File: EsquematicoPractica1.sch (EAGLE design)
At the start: 47 parts, among them IC1 GSOT05C-GS08, Q1 IRF7416PBF, Q2 IRF7416PBF, U1 MKL27Z64VLH4, U2 SFH6156-4TSMD-4_VO-L, U3 MC34063ADR, U4 SFH6156-4TSMD-4_VO-L, U5 SFH6156-4TSMD-4_VO-L, U6 SFH6156-4TSMD-4_VO-L, U7 5002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

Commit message: [Code] JTAG interface without pin connections
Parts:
- added J1: M50-3500542, M50-3500542:M50-3500542
- added R16: 10K, rcl:R-US_M1206
- renumbered U7 to TP5
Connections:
- new net N$32: R15.2
- new net N$33: R14.1
- new net N$34: J1.2, R16.1
- new net N$36: J1.4
- new net N$37: J1.6
- new net N$38: J1.8
- new net N$39: J1.10
- new net N$40: J1.1
- net GND: now also J1.3, J1.5
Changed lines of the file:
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@@
 <part name="GND12" library="supply1" library_urn="urn:adsk.eagle:library:371" deviceset="GND" device=""/>
 <part name="IC1" library="GSOT05C-GS08" deviceset="GSOT05C-GS08" device=""/>
-<part name="U7" library="5002" deviceset="5002" device=""/>
+<part name="TP5" library="5002" deviceset="5002" device=""/>
+<part name="R16" library="rcl" library_urn="urn:adsk.eagle:library:334" deviceset="R-US_" device="M1206" package3d_urn="urn:adsk.eagle:package:23566/1" value="10K"/>
+<part name="GND13" library="supply1" library_urn="urn:adsk.eagle:library:371" deviceset="GND" device=""/>
+<part name="J1" library="M50-3500542" deviceset="M50-3500542" device=""/>
 </parts>
 <sheets>
@@
 <sheet>
 <plain>
-<wire x1="129.54" y1="568.96" x2="1201.42" y2="568.96" width="0.1524" layer="97"/>
-<wire x1="129.54" y1="568.96" x2="129.54" y2="-160.02" width="0.1524" layer="97"/>
-<wire x1="129.54" y1="-160.02" x2="1201.42" y2="-160.02" width="0.1524" layer="97"/>
-<wire x1="1201.42" y1="568.96" x2="1201.42" y2="-160.02" width="0.1524" layer="97"/>
+<wire x1="129.54" y1="568.96" x2="264.16" y2="568.96" width="0.1524" layer="97"/>
+<wire x1="129.54" y1="568.96" x2="129.54" y2="439.42" width="0.1524" layer="97"/>
+<wire x1="129.54" y1="439.42" x2="264.16" y2="439.42" width="0.1524" layer="97"/>
+<wire x1="264.16" y1="568.96" x2="264.16" y2="439.42" width="0.1524" layer="97"/>
+<wire x1="266.7" y1="568.96" x2="401.32" y2="568.96" width="0.1524" layer="97"/>
+<wire x1="266.7" y1="568.96" x2="266.7" y2="439.42" width="0.1524" layer="97"/>
+<wire x1="266.7" y1="439.42" x2="401.32" y2="439.42" width="0.1524" layer="97"/>
+<wire x1="401.32" y1="568.96" x2="401.32" y2="439.42" width="0.1524" layer="97"/>
 </plain>
 <instances>
@@
 <instance part="GND12" gate="1" x="210.82" y="553.72" rot="R180"/>
 <instance part="IC1" gate="G$1" x="210.82" y="510.54" rot="R90"/>
-<instance part="U7" gate="G$1" x="213.36" y="482.6" rot="R270"/>
+<instance part="TP5" gate="G$1" x="213.36" y="482.6" rot="R270"/>
+<instance part="R16" gate="G$1" x="365.76" y="508" rot="R90"/>
+<instance part="GND13" gate="1" x="320.04" y="485.14"/>
+<instance part="J1" gate="G$1" x="325.12" y="500.38"/>
 </instances>
 <busses>
@@
 <junction x="210.82" y="551.18"/>
 </segment>
+<segment>
+<pinref part="J1" gate="G$1" pin="3"/>
+<wire x1="325.12" y1="497.84" x2="320.04" y2="497.84" width="0.1524" layer="91"/>
+<wire x1="320.04" y1="497.84" x2="320.04" y2="495.3" width="0.1524" layer="91"/>
+<pinref part="J1" gate="G$1" pin="5"/>
+<wire x1="320.04" y1="495.3" x2="320.04" y2="487.68" width="0.1524" layer="91"/>
+<wire x1="325.12" y1="495.3" x2="320.04" y2="495.3" width="0.1524" layer="91"/>
+<junction x="320.04" y="495.3"/>
+<pinref part="GND13" gate="1" pin="GND"/>
+</segment>
 </net>
 <net name="N$26" class="0">
 <segment>
 <pinref part="L3" gate="G$1" pin="2"/>
-<pinref part="U7" gate="G$1" pin="1"/>
+<pinref part="TP5" gate="G$1" pin="1"/>
 <wire x1="205.74" y1="482.6" x2="213.36" y2="482.6" width="0.1524" layer="91"/>
-<wire x1="213.36" y1="482.6" x2="236.22" y2="482.6" width="0.1524" layer="91"/>
+<wire x1="213.36" y1="482.6" x2="248.92" y2="482.6" width="0.1524" layer="91"/>
 <junction x="213.36" y="482.6"/>
 </segment>
 </net>
+<net name="N$32" class="0">
+<segment>
+<pinref part="R15" gate="G$1" pin="2"/>
+<wire x1="228.6" y1="497.84" x2="248.92" y2="497.84" width="0.1524" layer="91"/>
+</segment>
+</net>
+<net name="N$33" class="0">
+<segment>
+<pinref part="R14" gate="G$1" pin="1"/>
+<wire x1="236.22" y1="492.76" x2="248.92" y2="492.76" width="0.1524" layer="91"/>
+</segment>
+</net>
+<net name="N$34" class="0">
+<segment>
+<pinref part="J1" gate="G$1" pin="2"/>
+<pinref part="R16" gate="G$1" pin="1"/>
+<wire x1="347.98" y1="500.38" x2="365.76" y2="500.38" width="0.1524" layer="91"/>
+<wire x1="365.76" y1="500.38" x2="365.76" y2="502.92" width="0.1524" layer="91"/>
+<wire x1="365.76" y1="500.38" x2="381" y2="500.38" width="0.1524" layer="91"/>
+<junction x="365.76" y="500.38"/>
+</segment>
+</net>
+<net name="N$36" class="0">
+<segment>
+<pinref part="J1" gate="G$1" pin="4"/>
+<wire x1="347.98" y1="497.84" x2="381" y2="497.84" width="0.1524" layer="91"/>
+</segment>
+</net>
+<net name="N$37" class="0">
+<segment>
+<pinref part="J1" gate="G$1" pin="6"/>
+<wire x1="347.98" y1="495.3" x2="381" y2="495.3" width="0.1524" layer="91"/>
+</segment>
+</net>
+<net name="N$38" class="0">
+<segment>
+<pinref part="J1" gate="G$1" pin="8"/>
+<wire x1="347.98" y1="492.76" x2="381" y2="492.76" width="0.1524" layer="91"/>
+</segment>
+</net>
+<net name="N$39" class="0">
+<segment>
+<pinref part="J1" gate="G$1" pin="10"/>
+<wire x1="347.98" y1="490.22" x2="381" y2="490.22" width="0.1524" layer="91"/>
+</segment>
+</net>
+<net name="N$40" class="0">
+<segment>
+<pinref part="J1" gate="G$1" pin="1"/>
+<wire x1="325.12" y1="500.38" x2="320.04" y2="500.38" width="0.1524" layer="91"/>
+<wire x1="320.04" y1="500.38" x2="320.04" y2="502.92" width="0.1524" layer="91"/>
+</segment>
+</net>

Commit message: [Code] Cristal circuit finished and
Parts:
- added C42, C43: 12PF, GRM1555C1H120JA01D:GRM1555C1H120JA01D
- added R81: 10M, RK73H1JLTD1005F:RK73H1JLTD1005F
- added Y3: 32.768KHZ, ABS25-32.768KHZ-T:ABS25-32.768KHZ-T
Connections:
- new net N$35: C42.1, R81.1, Y3.3
- new net N$41: C43.1, Y3.4
- net GND: now also C42.2, C43.2
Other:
- moved on the sheet: IC1, L3, L4, R14, R15, TP5, X1G$1, X1S

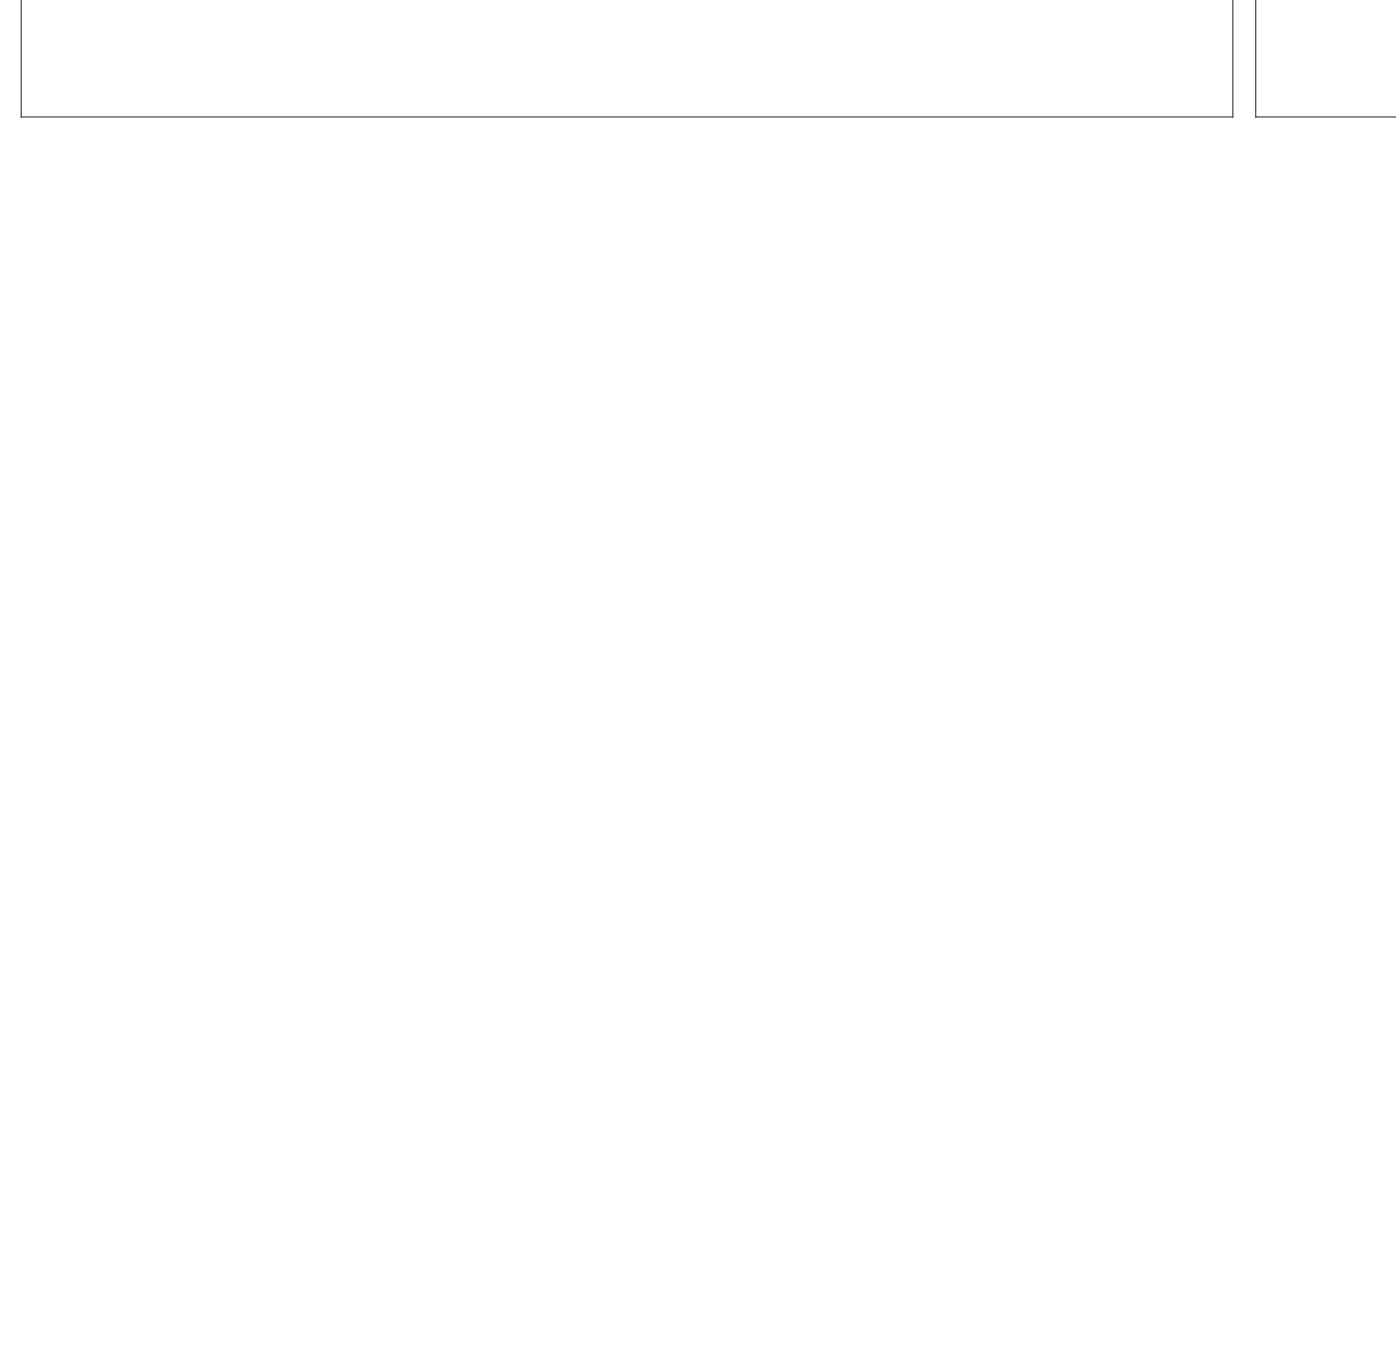
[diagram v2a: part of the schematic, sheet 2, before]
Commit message: [code] TLV274QPWRG4Q1
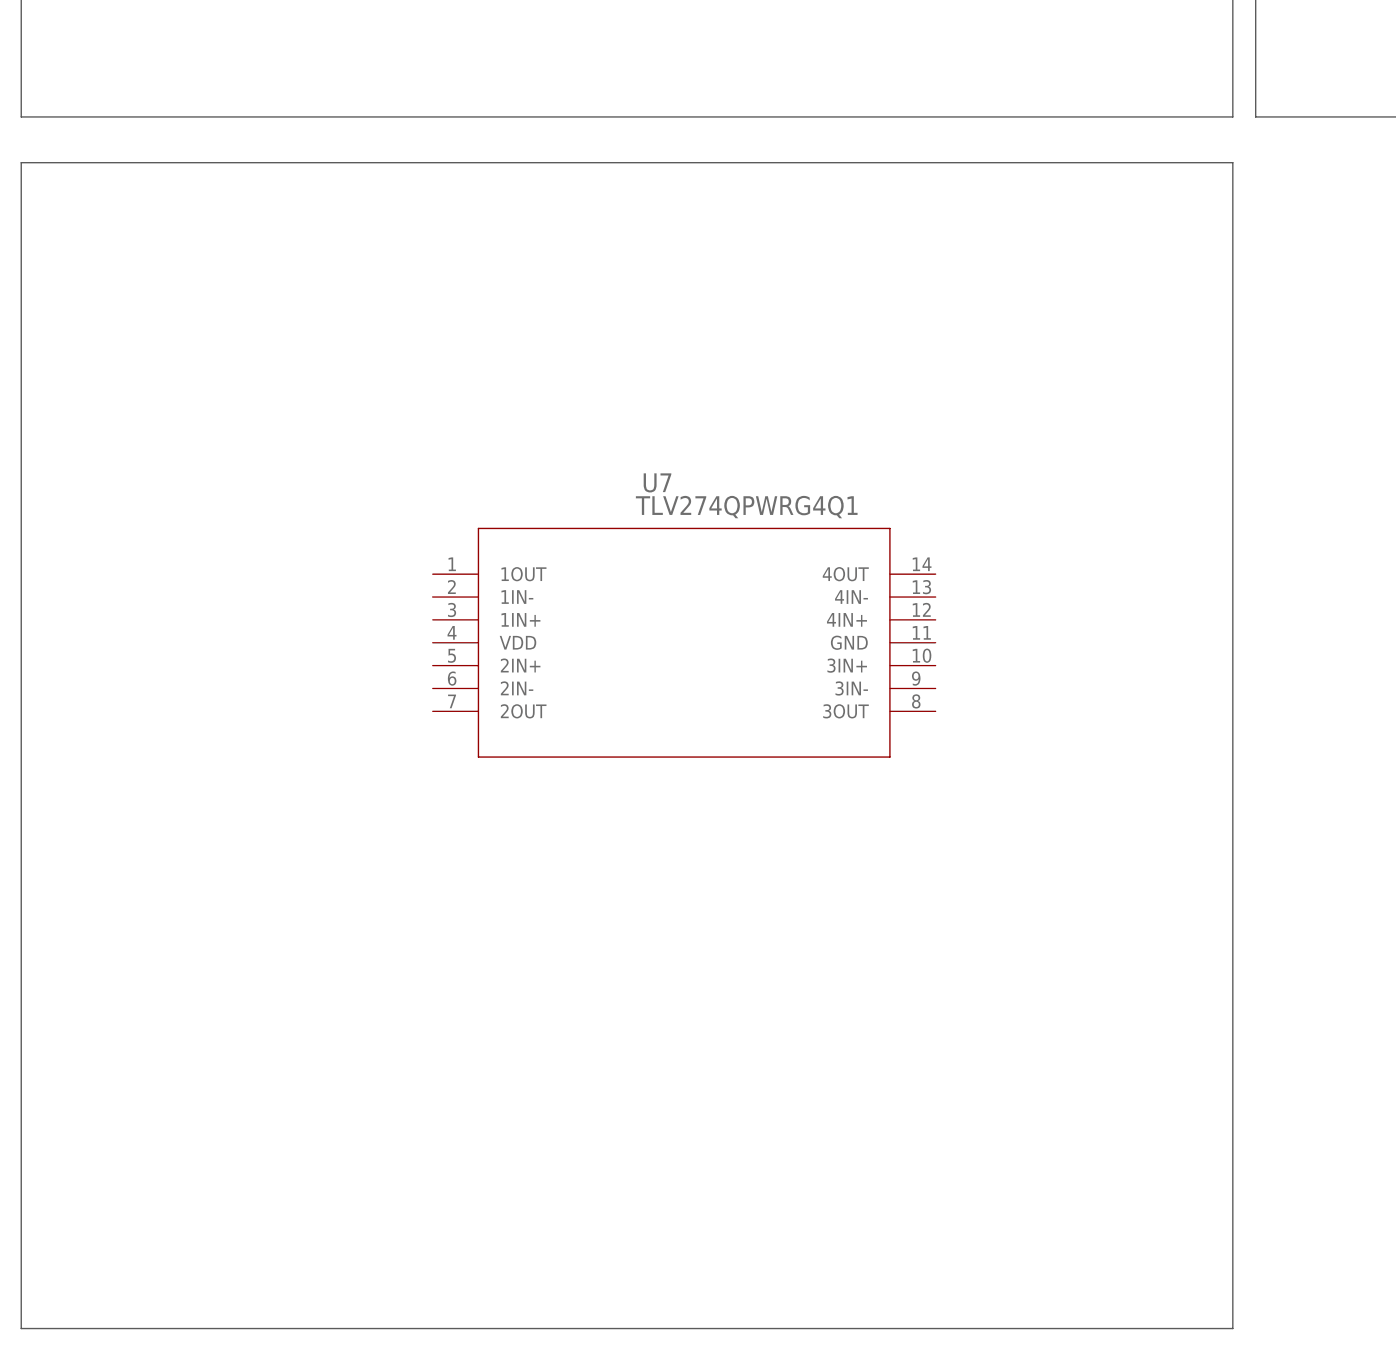
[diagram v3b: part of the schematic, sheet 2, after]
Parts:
- added U7: TLV274QPWRG4Q1, TLV274QPWRG4Q1:TLV274QPWRG4Q1
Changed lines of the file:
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@@
 <part name="GND14" library="supply1" library_urn="urn:adsk.eagle:library:371" deviceset="GND" device=""/>
 <part name="R81" library="RK73H1JLTD1005F" deviceset="RK73H1JLTD1005F" device="" value="10M"/>
+<part name="U7" library="TLV274QPWRG4Q1" deviceset="TLV274QPWRG4Q1" device=""/>
 </parts>
 <sheets>
@@
 <wire x1="403.86" y1="439.42" x2="538.48" y2="439.42" width="0.1524" layer="97"/>
 <wire x1="538.48" y1="568.96" x2="538.48" y2="439.42" width="0.1524" layer="97"/>
+<wire x1="129.54" y1="434.34" x2="264.16" y2="434.34" width="0.1524" layer="97"/>
+<wire x1="129.54" y1="434.34" x2="129.54" y2="304.8" width="0.1524" layer="97"/>
+<wire x1="129.54" y1="304.8" x2="264.16" y2="304.8" width="0.1524" layer="97"/>
+<wire x1="264.16" y1="434.34" x2="264.16" y2="304.8" width="0.1524" layer="97"/>
 </plain>
 <instances>
@@
 <instance part="GND14" gate="1" x="505.46" y="502.92"/>
 <instance part="R81" gate="G$1" x="429.26" y="530.86" rot="R270"/>
+<instance part="U7" gate="A" x="172.72" y="388.62"/>
 </instances>
 <busses>

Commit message: Merge remote-tracking branch 'origin/master'
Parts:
- renumbered R14 to R101, R15 to R100, R16 to R102
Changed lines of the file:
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@@
 <part name="3.3V1" library="con-ptr500" library_urn="urn:adsk.eagle:library:181" deviceset="AK300/2" device="" package3d_urn="urn:adsk.eagle:package:9881/1"/>
 <part name="X1" library="con-cypressindustries" library_urn="urn:adsk.eagle:library:138" deviceset="MINI-USB-SCHIELD-" device="32005-201" package3d_urn="urn:adsk.eagle:package:6443/1"/>
-<part name="R14" library="rcl" library_urn="urn:adsk.eagle:library:334" deviceset="R-US_" device="M1206" package3d_urn="urn:adsk.eagle:package:23566/1" value="33"/>
-<part name="R15" library="rcl" library_urn="urn:adsk.eagle:library:334" deviceset="R-US_" device="M1206" package3d_urn="urn:adsk.eagle:package:23566/1" value="33"/>
+<part name="R101" library="rcl" library_urn="urn:adsk.eagle:library:334" deviceset="R-US_" device="M1206" package3d_urn="urn:adsk.eagle:package:23566/1" value="33"/>
+<part name="R100" library="rcl" library_urn="urn:adsk.eagle:library:334" deviceset="R-US_" device="M1206" package3d_urn="urn:adsk.eagle:package:23566/1" value="33"/>
 <part name="L3" library="MPZ2012S331AT000" deviceset="MPZ2012S331AT000" device="" value="MPZ2012S331A"/>
 <part name="L4" library="MPZ2012S331AT000" deviceset="MPZ2012S331AT000" device="" value="MPZ2012S331A"/>
@@
 <part name="IC1" library="GSOT05C-GS08" deviceset="GSOT05C-GS08" device=""/>
 <part name="TP5" library="5002" deviceset="5002" device=""/>
-<part name="R16" library="rcl" library_urn="urn:adsk.eagle:library:334" deviceset="R-US_" device="M1206" package3d_urn="urn:adsk.eagle:package:23566/1" value="10K"/>
+<part name="R102" library="rcl" library_urn="urn:adsk.eagle:library:334" deviceset="R-US_" device="M1206" package3d_urn="urn:adsk.eagle:package:23566/1" value="10K"/>
 <part name="GND13" library="supply1" library_urn="urn:adsk.eagle:library:371" deviceset="GND" device=""/>
 <part name="J1" library="M50-3500542" deviceset="M50-3500542" device=""/>
@@
 <instance part="X1" gate="G$1" x="142.24" y="505.46" rot="R180"/>
 <instance part="X1" gate="S" x="142.24" y="515.62" rot="R180"/>
-<instance part="R14" gate="G$1" x="210.82" y="500.38" rot="R180"/>
-<instance part="R15" gate="G$1" x="203.2" y="505.46"/>
+<instance part="R101" gate="G$1" x="210.82" y="500.38" rot="R180"/>
+<instance part="R100" gate="G$1" x="203.2" y="505.46"/>
 <instance part="L3" gate="G$1" x="165.1" y="490.22"/>
 <instance part="L4" gate="G$1" x="152.4" y="548.64"/>
@@
 <instance part="IC1" gate="G$1" x="190.5" y="508" rot="R90"/>
 <instance part="TP5" gate="G$1" x="193.04" y="490.22" rot="R270"/>
-<instance part="R16" gate="G$1" x="365.76" y="508" rot="R90"/>
+<instance part="R102" gate="G$1" x="365.76" y="508" rot="R90"/>
 <instance part="GND13" gate="1" x="320.04" y="485.14"/>
 <instance part="J1" gate="G$1" x="325.12" y="500.38"/>
@@
 <pinref part="X1" gate="G$1" pin="3"/>
 <wire x1="147.32" y1="505.46" x2="193.04" y2="505.46" width="0.1524" layer="91"/>
-<pinref part="R15" gate="G$1" pin="1"/>
+<pinref part="R100" gate="G$1" pin="1"/>
 <pinref part="IC1" gate="G$1" pin="CATHODE(2)"/>
 <wire x1="193.04" y1="505.46" x2="198.12" y2="505.46" width="0.1524" layer="91"/>
@@
 <wire x1="165.1" y1="502.92" x2="165.1" y2="500.38" width="0.1524" layer="91"/>
 <wire x1="165.1" y1="500.38" x2="190.5" y2="500.38" width="0.1524" layer="91"/>
-<pinref part="R14" gate="G$1" pin="2"/>
+<pinref part="R101" gate="G$1" pin="2"/>
 <pinref part="IC1" gate="G$1" pin="CATHODE(1)"/>
 <wire x1="190.5" y1="500.38" x2="205.74" y2="500.38" width="0.1524" layer="91"/>
@@
 <net name="N$32" class="0">
 <segment>
-<pinref part="R15" gate="G$1" pin="2"/>
+<pinref part="R100" gate="G$1" pin="2"/>
 <wire x1="208.28" y1="505.46" x2="228.6" y2="505.46" width="0.1524" layer="91"/>
 </segment>
@@
 <net name="N$33" class="0">
 <segment>
-<pinref part="R14" gate="G$1" pin="1"/>
+<pinref part="R101" gate="G$1" pin="1"/>
 <wire x1="215.9" y1="500.38" x2="228.6" y2="500.38" width="0.1524" layer="91"/>
 </segment>
@@
 <segment>
 <pinref part="J1" gate="G$1" pin="2"/>
-<pinref part="R16" gate="G$1" pin="1"/>
+<pinref part="R102" gate="G$1" pin="1"/>
 <wire x1="347.98" y1="500.38" x2="365.76" y2="500.38" width="0.1524" layer="91"/>
 <wire x1="365.76" y1="500.38" x2="365.76" y2="502.92" width="0.1524" layer="91"/>
